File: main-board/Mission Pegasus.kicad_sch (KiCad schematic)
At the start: 28 parts, among them J1 TC2030, Q1 DTC113Z, U2 4MB Flash, U3 AS72652, U4 AS72653, U6 AS72651

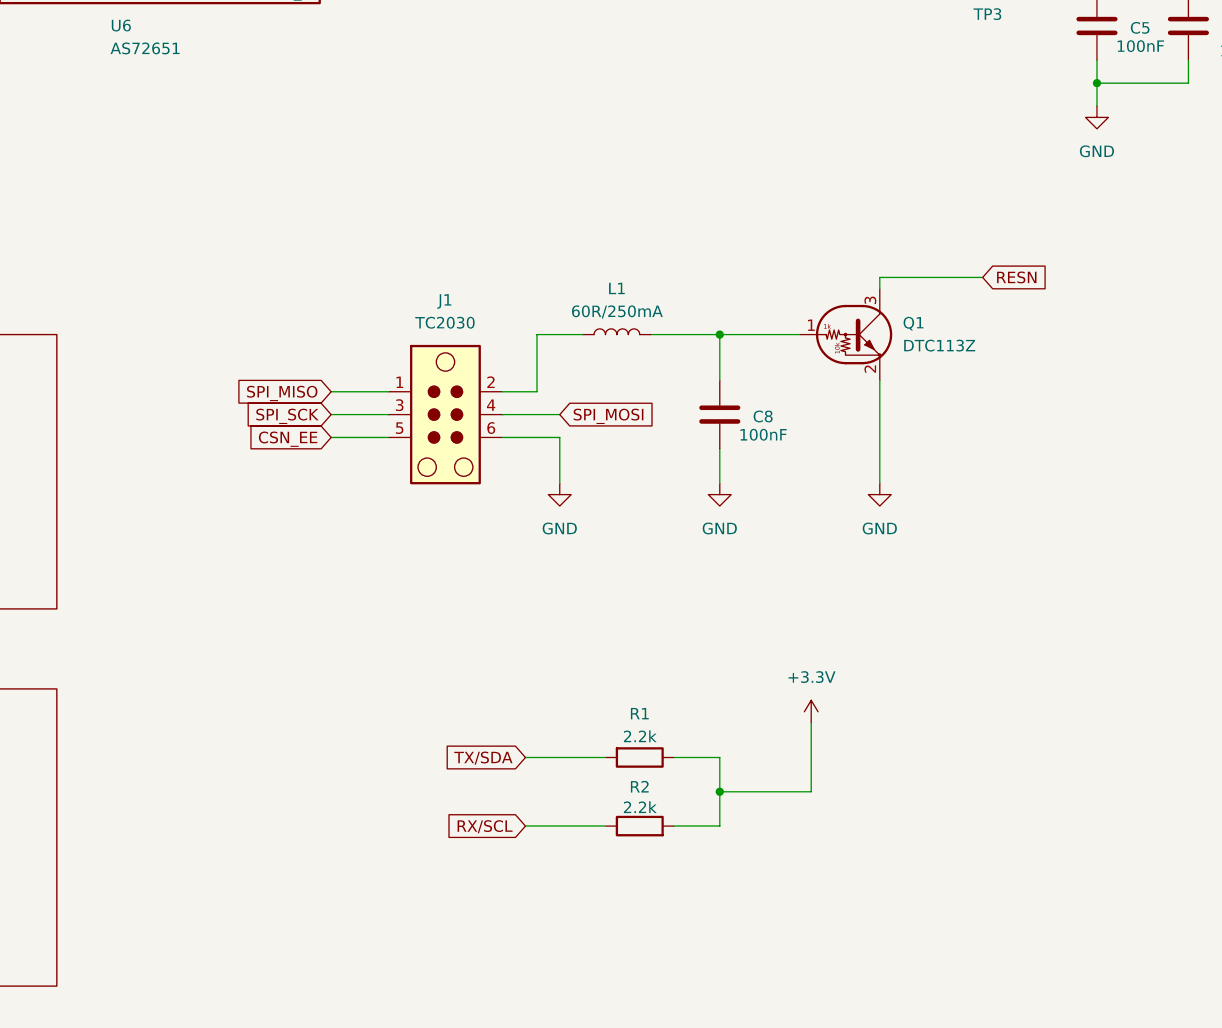
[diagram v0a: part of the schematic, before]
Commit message: Add Samtec FTSH-105-04-L-D-RA and SFMC-105-01-L-D to both boards
Import two Library Loader parts (a 2x5 1.27mm right-angle header and its
mating 2x5 socket strip) into the SamacSys_Parts library of BOTH the main
board and the mezzanine board: footprints, 3D models, and symbols
appended. 3D paths rewritten to ${KIPRJMOD}-relative and each symbol's
Footprint property qualified with the library nickname.
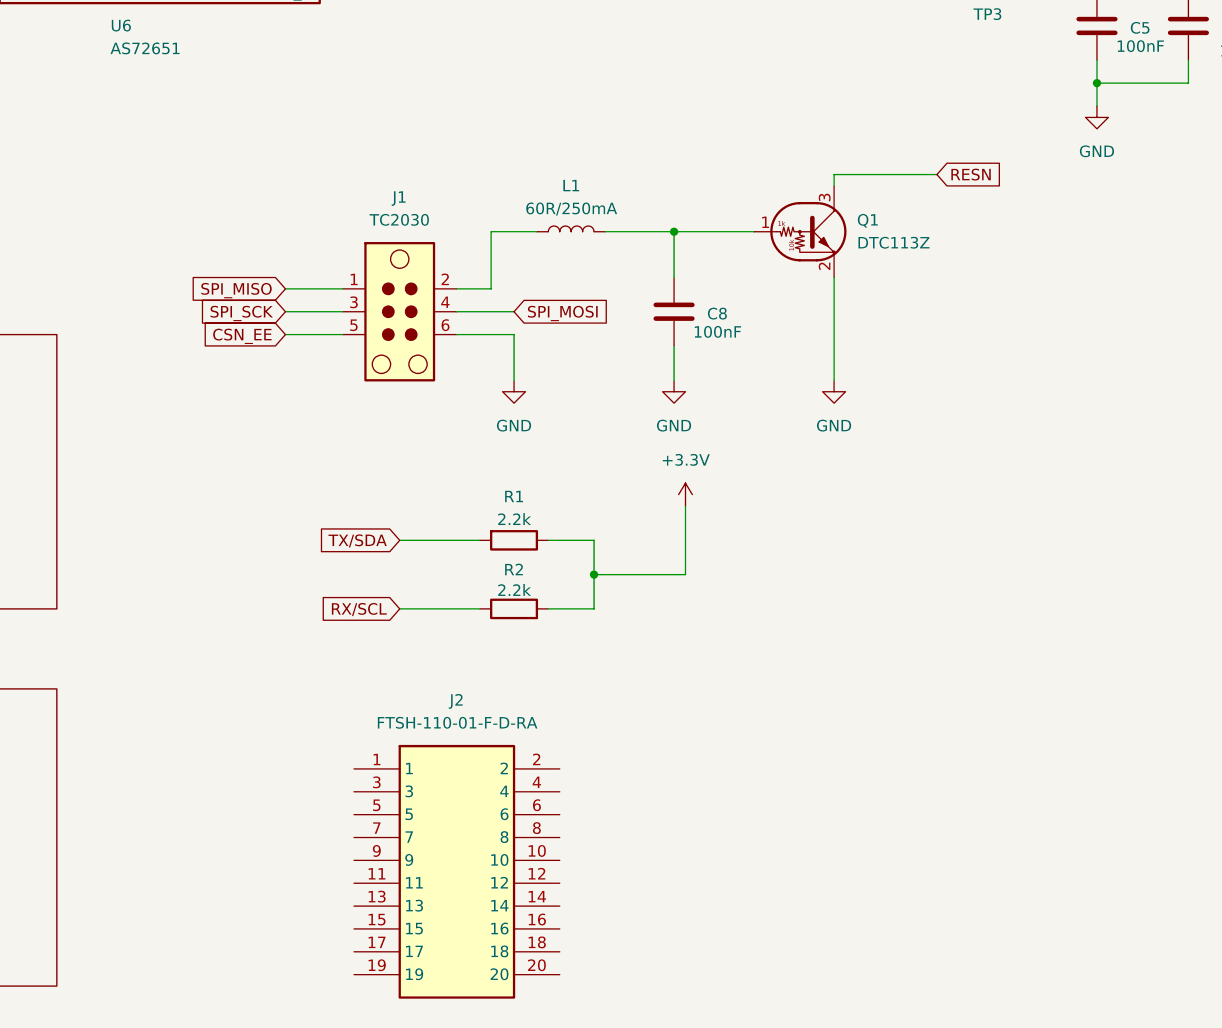
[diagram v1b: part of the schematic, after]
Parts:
- added J2: FTSH-110-01-F-D-RA, SamacSys_Parts:FTSH-110-XX-YYY-D-RA, symbol SamacSys_Parts:FTSH-110-01-F-D-RA
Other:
- moved on the sheet: C8, J1, L1, Q1, R1, R2

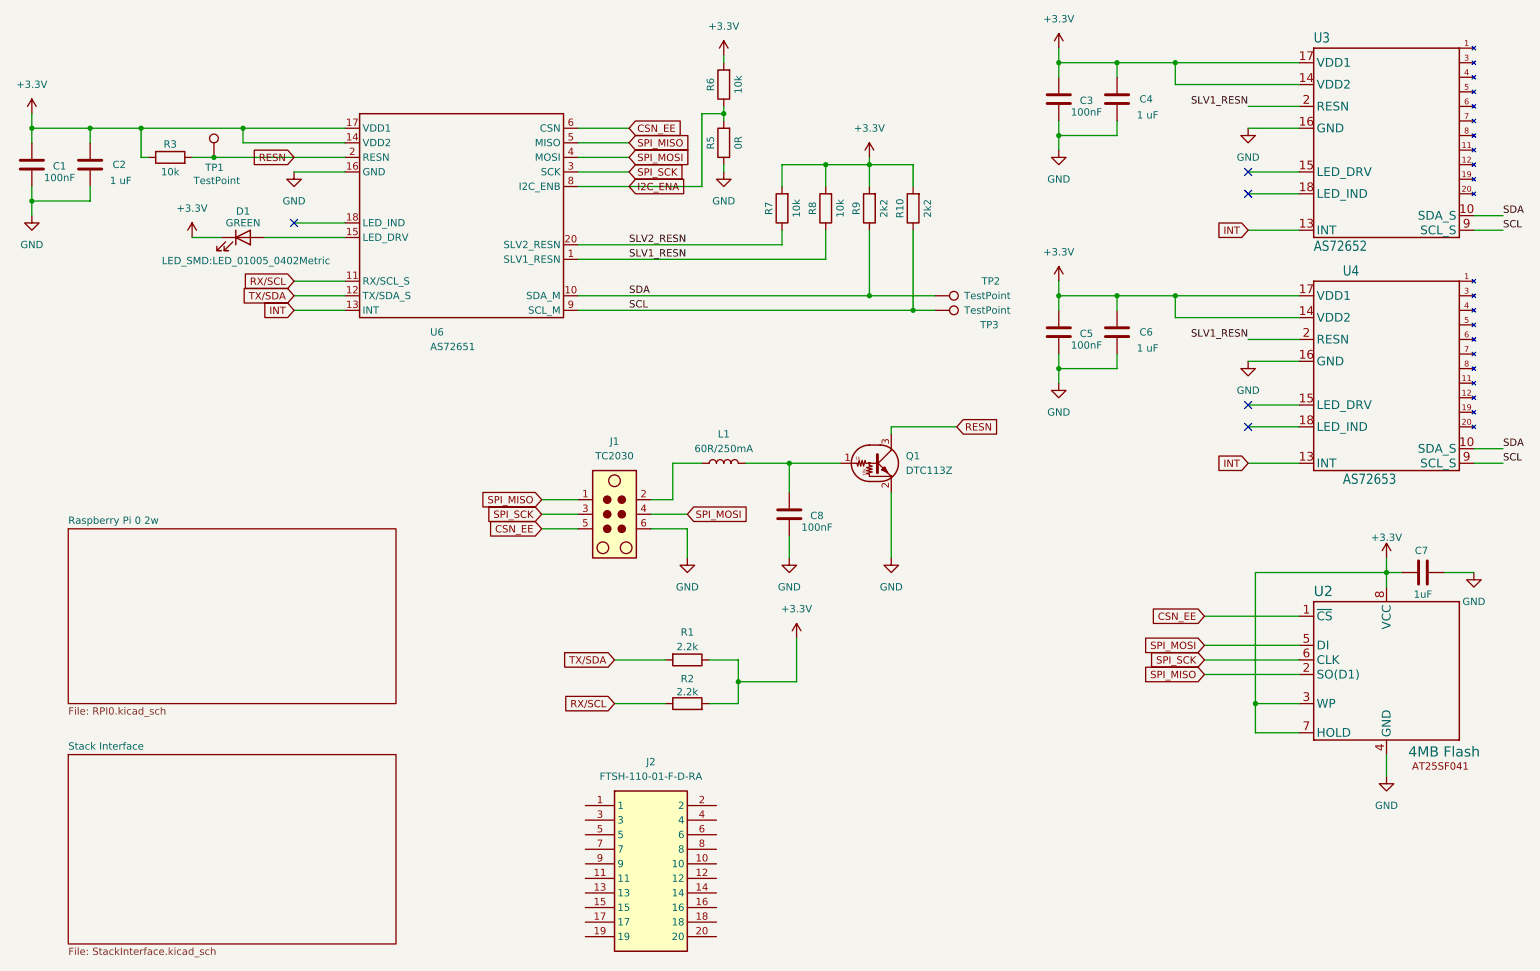
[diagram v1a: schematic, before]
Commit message: Attach Raspberry Pi Zero 2 W 3D model to RPi footprint
Add the mechanical STEP model of the Raspberry Pi Zero 2 W board
(RaspberryPi_Zero_2W.step, from the downloaded SolidWorks CAD) to
main-board 3dmodels, and reference it from the RASPBERRYPI-ZERO_RPI-ZERO
footprint via a ${KIPRJMOD}-relative path. Offset/rotation set to zero as
a starting point - needs alignment tuning in KiCad's 3D tab.
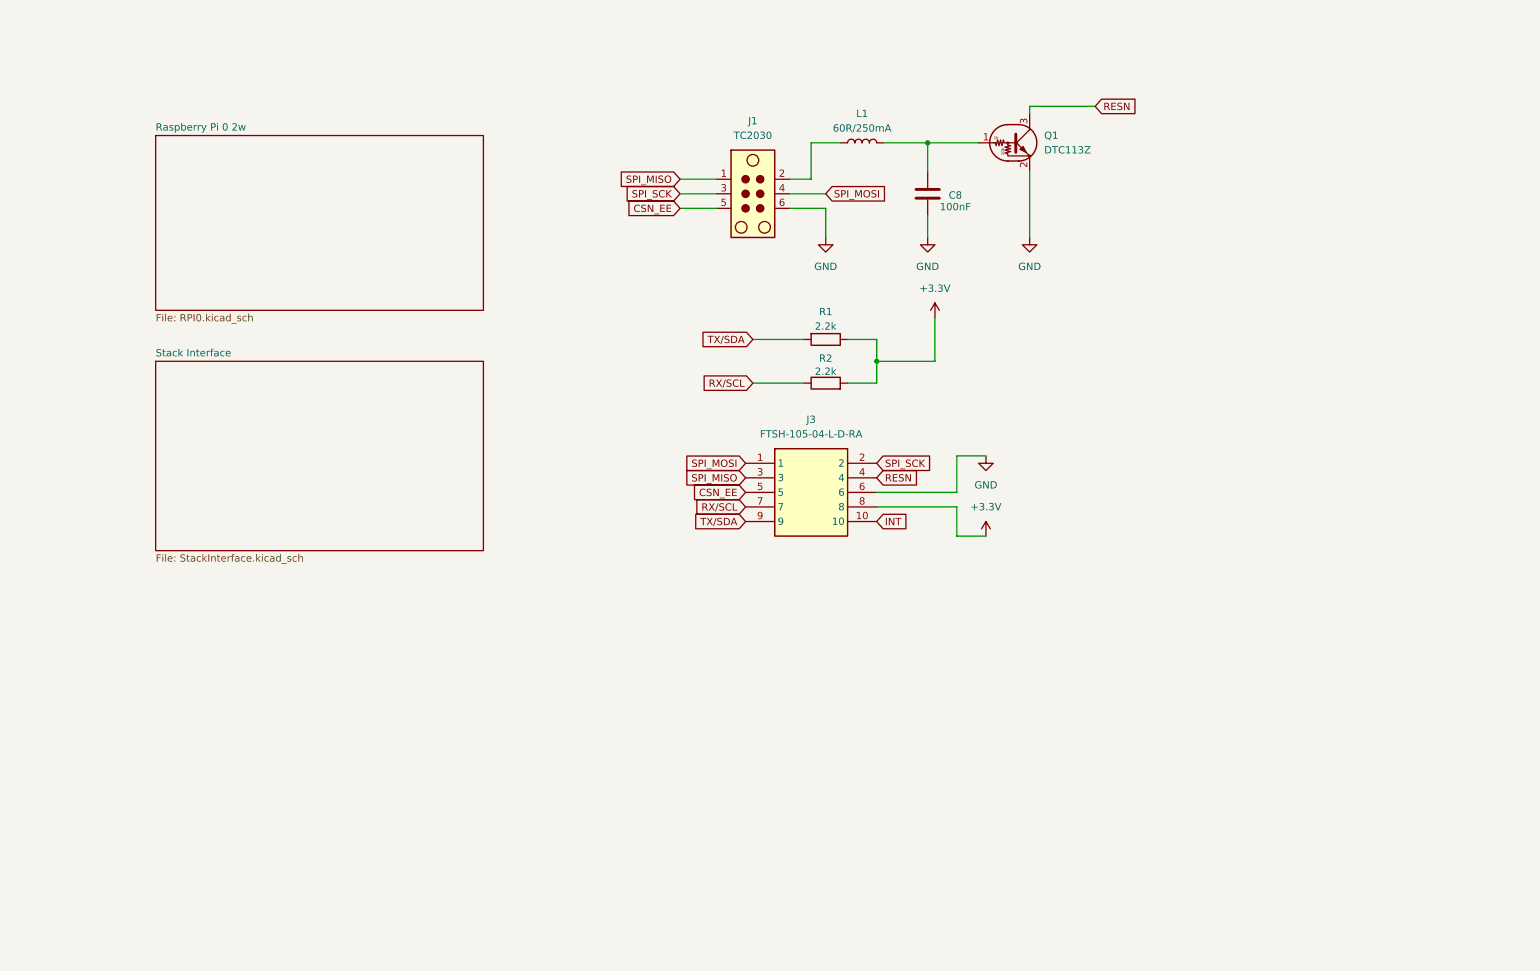
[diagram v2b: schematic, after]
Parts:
- removed C1, C3, C5: 100nF, SparkfunLibrary:0603, symbol Device:C
- removed C2, C4, C6: 1 uF, SparkfunLibrary:0603, symbol Device:C
- removed C7: 1uF, SparkfunLibrary:0603, symbol Device:C
- removed D1: GREEN, LED_SMD:LED_01005_0402Metric, symbol Device:LED
- removed J2: FTSH-110-01-F-D-RA, SamacSys_Parts:FTSH-110-XX-YYY-D-RA, symbol SamacSys_Parts:FTSH-110-01-F-D-RA
- removed R10, R9: 2k2, SparkfunLibrary:0603, symbol Device:R
- removed R3, R6, R7, R8: 10k, SparkfunLibrary:0603, symbol Device:R
- removed R5: 0R, SparkfunLibrary:0603, symbol Device:R
- removed TP1, TP2, TP3: TestPoint, TestPoint:TestPoint_Pad_D1.0mm, symbol Connector:TestPoint
- removed U2: 4MB Flash, SparkfunLibrary:4MbFlash, symbol Qwiic_Spectral_Sensor-AS7265x-eagle-import:AT25SF041
- removed U3: AS72652, SparkfunLibrary:AS72651, symbol Qwiic_Spectral_Sensor-AS7265x-eagle-import:AS72652
- removed U4: AS72653, SparkfunLibrary:AS72651, symbol Qwiic_Spectral_Sensor-AS7265x-eagle-import:AS72653
- removed U6: AS72651, Package_LGA:AMS_LGA-20_4.7x4.5mm_P0.65mm, symbol Sensor_Optical:AS72651
- added J3: FTSH-105-04-L-D-RA, SamacSys_Parts:FTSH-105-XX-YYY-D-RA, symbol SamacSys_Parts:FTSH-105-04-L-D-RA
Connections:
- net +3.3V: now also J3.8
- net CSN_EE: now also J3.5
- net GND: now also J3.6
- net INT: now also J3.10
- net RESN: now also J3.4
- net RX/SCL: now also J3.7
- net SPI_MISO: now also J3.3
- net SPI_MOSI: now also J3.1
- net SPI_SCK: now also J3.2
- net TX/SDA: now also J3.9
- no-connect marks 5 -> 0
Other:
- moved on the sheet: C8, J1, L1, Q1, R1, R2

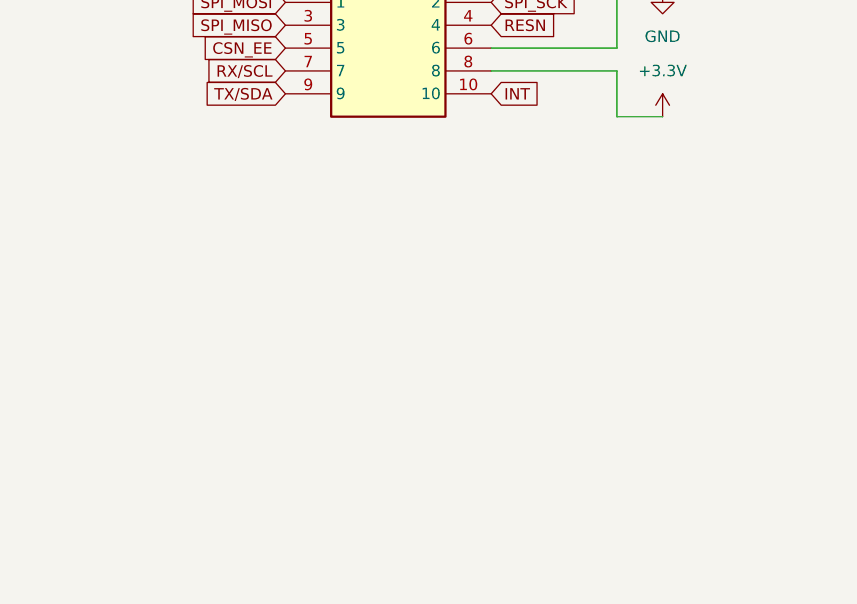
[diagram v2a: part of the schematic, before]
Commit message: Add J4 and J5 sensor-board connectors (3 parallel positions)
Add two more FTSH-105-04-L-D-RA connectors (J4, J5) alongside J3 on the
main board so the 90-degree sensor board can mount in three interchangeable
positions, wired in parallel to the same nets. Includes associated power
and decoupling.
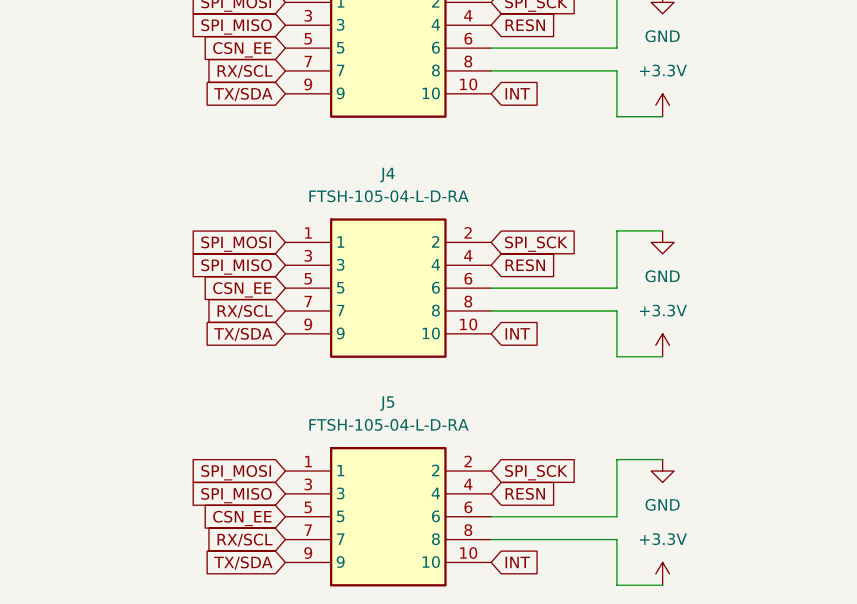
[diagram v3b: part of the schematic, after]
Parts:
- added J4, J5: FTSH-105-04-L-D-RA, SamacSys_Parts:FTSH-105-XX-YYY-D-RA, symbol SamacSys_Parts:FTSH-105-04-L-D-RA
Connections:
- net +3.3V: now also J4.8, J5.8
- net CSN_EE: now also J4.5, J5.5
- net GND: now also J4.6, J5.6
- net INT: now also J4.10, J5.10
- net RESN: now also J4.4, J5.4
- net RX/SCL: now also J4.7, J5.7
- net SPI_MISO: now also J4.3, J5.3
- net SPI_MOSI: now also J4.1, J5.1
- net SPI_SCK: now also J4.2, J5.2
- net TX/SDA: now also J4.9, J5.9

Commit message: Add Vishay CRCW06032K20FKEA (2.2k 0603) to mezzanine libraries
Import the Library Loader part (2.2k ohm 0603 resistor) into the
mezzanine's SamacSys_Parts library: footprint, 3D model, and symbol
appended. 3D path rewritten to ${KIPRJMOD}-relative and the symbol's
Footprint property qualified with the library nickname.
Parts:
- added H3, H4, H5, H6, H7, H8: MountingHole, Mounting_Wuerth:Mounting_Wuerth_WA-SMSI-M2.5_H0.5mm_9774005151, symbol Mechanical:MountingHole

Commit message: Update larger board design
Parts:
- H3, H4, H5, H6, H7, H8: footprint Mounting_Wuerth:Mounting_Wuerth_WA-SMSI-M2.5_H0.5mm_9774005151 -> MountingHole:MountingHole_2.7mm_M2.5
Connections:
- net CSN_EE: now also J3.1, J4.1, J5.1; no longer J3.5, J4.5, J5.5
- net GND: now also J3.10, J4.10, J5.10; no longer J3.6, J4.6, J5.6
- net INT: now also J3.6, J4.6, J5.6; no longer J3.10, J4.10, J5.10
- net RESN: now also J3.9, J4.9, J5.9; no longer J3.4, J4.4, J5.4
- net RX/SCL: now also J3.2, J4.2, J5.2; no longer J3.7, J4.7, J5.7
- net SPI_MOSI: now also J3.5, J4.5, J5.5; no longer J3.1, J4.1, J5.1
- net SPI_SCK: now also J3.7, J4.7, J5.7; no longer J3.2, J4.2, J5.2
- net TX/SDA: now also J3.4, J4.4, J5.4; no longer J3.9, J4.9, J5.9

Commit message: Moved RA connectors back to 16mm away
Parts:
- H3, H4, H5, H6, H7, H8: footprint MountingHole:MountingHole_2.7mm_M2.5 -> MountingHole:MountingHole_3.2mm_M3
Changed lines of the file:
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@@
 			)
 		)
-		(property "Footprint" "MountingHole:MountingHole_2.7mm_M2.5"
+		(property "Footprint" "MountingHole:MountingHole_3.2mm_M3"
 			(at 41.91 163.83 0)
 			(hide yes)
@@
 			)
 		)
-		(property "Footprint" "MountingHole:MountingHole_2.7mm_M2.5"
+		(property "Footprint" "MountingHole:MountingHole_3.2mm_M3"
 			(at 41.91 140.97 0)
 			(hide yes)
@@
 			)
 		)
-		(property "Footprint" "MountingHole:MountingHole_2.7mm_M2.5"
+		(property "Footprint" "MountingHole:MountingHole_3.2mm_M3"
 			(at 41.91 125.73 0)
 			(hide yes)
@@
 			)
 		)
-		(property "Footprint" "MountingHole:MountingHole_2.7mm_M2.5"
+		(property "Footprint" "MountingHole:MountingHole_3.2mm_M3"
 			(at 41.91 148.59 0)
 			(hide yes)
@@
 			)
 		)
-		(property "Footprint" "MountingHole:MountingHole_2.7mm_M2.5"
+		(property "Footprint" "MountingHole:MountingHole_3.2mm_M3"
 			(at 41.91 156.21 0)
 			(hide yes)
@@
 			)
 		)
-		(property "Footprint" "MountingHole:MountingHole_2.7mm_M2.5"
+		(property "Footprint" "MountingHole:MountingHole_3.2mm_M3"
 			(at 41.91 133.35 0)
 			(hide yes)
